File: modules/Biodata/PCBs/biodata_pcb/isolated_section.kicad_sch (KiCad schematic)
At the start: 12 parts, among them U1 NE555P, U3 TEA1-0505, U4 PC817

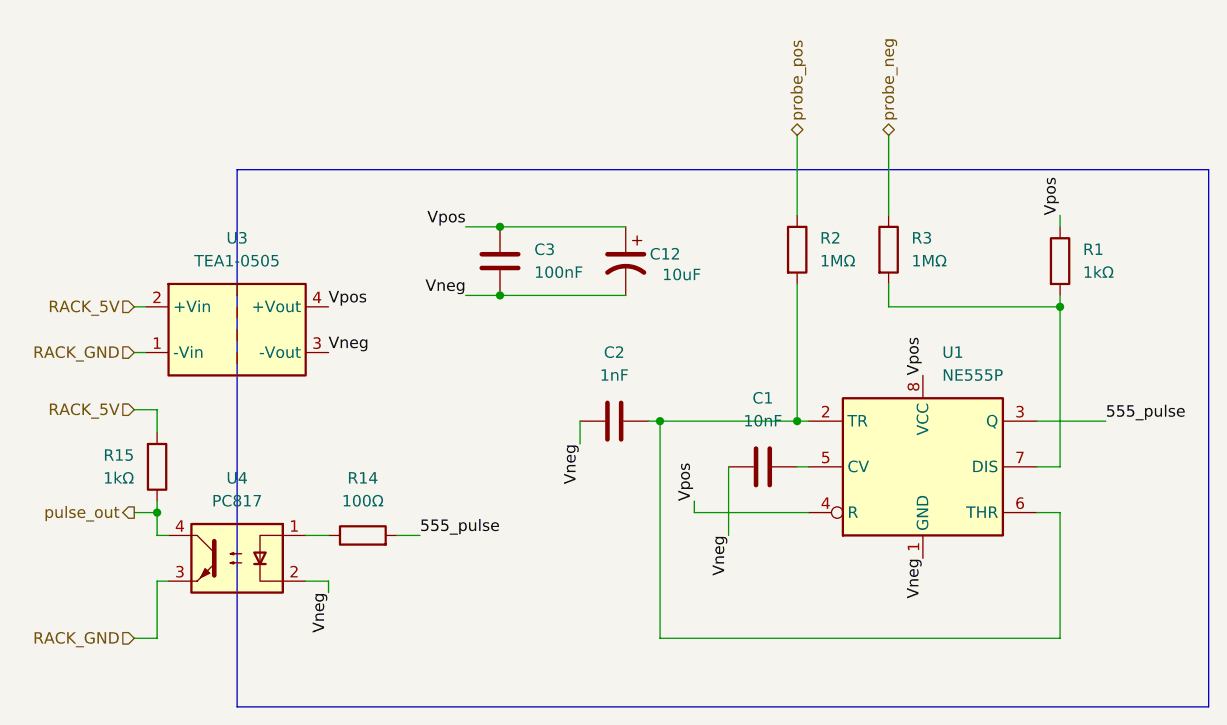
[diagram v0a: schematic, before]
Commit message: Switch biodata to monophonic
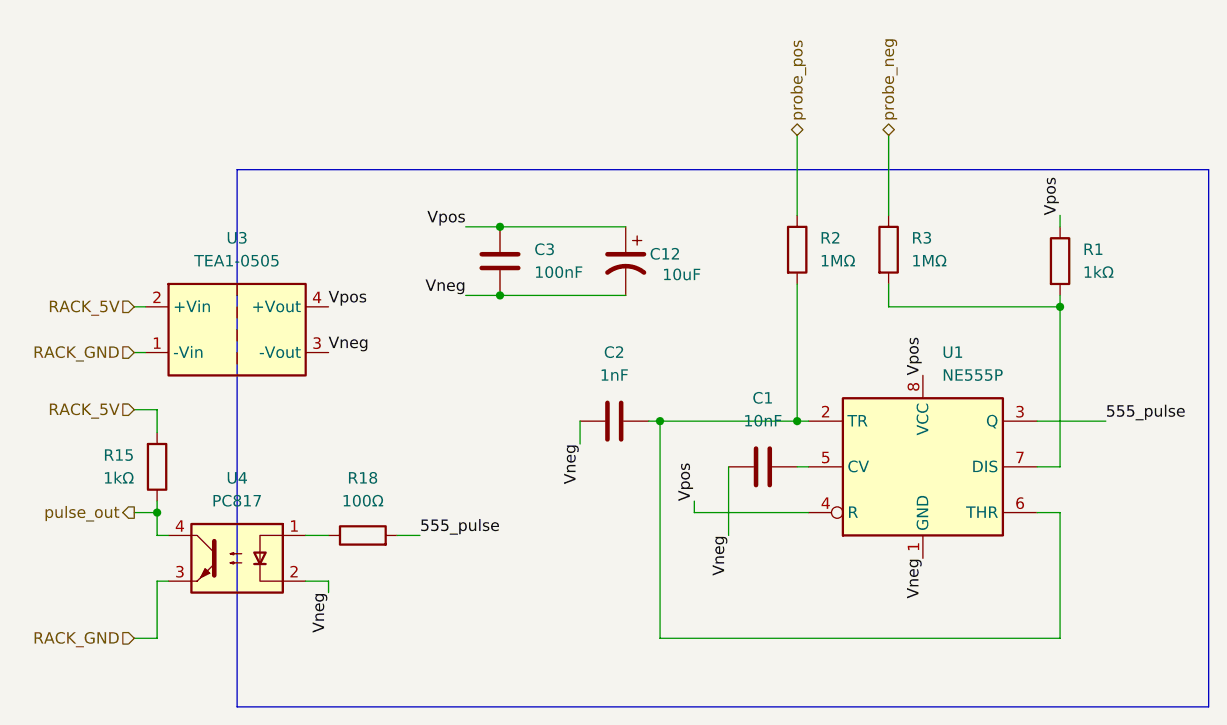
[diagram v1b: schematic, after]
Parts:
- renumbered R14 to R18
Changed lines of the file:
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@@
 	(title_block
 		(title "Biodata")
-		(date "2025-08-07")
-		(rev "v0.1")
+		(date "2025-10-11")
+		(rev "v0.2")
 		(company "Free Modular")
 	)
@@
 		(dnp no)
 		(fields_autoplaced yes)
-		(property "Reference" "R14"
+		(property "Reference" "R18"
 			(at 64.77 82.55 90)
 			(effects
@@
 			(project "biodata_pcb"
 				(path "/b52d098f-d782-4794-942d-95fe9e334d06/c75a632f-e661-4484-8d06-5c636c2b505d/afacce7b-5b17-4257-bd34-0cb53028cdba"
-					(reference "R14")
+					(reference "R18")
 					(unit 1)
 				)
